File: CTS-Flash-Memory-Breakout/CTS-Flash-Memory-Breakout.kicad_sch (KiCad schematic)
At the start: 8 parts, among them J1 Conn_02x07_Counter_Clockwise, U1 S70FL01GSAGMFI011

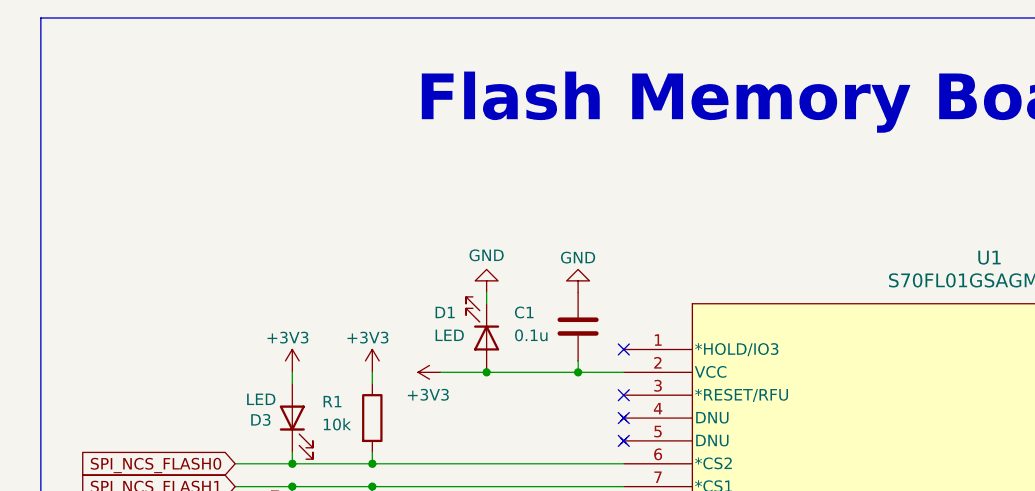
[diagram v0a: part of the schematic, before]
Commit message: Update errata on schematic, add rendering and part number to README
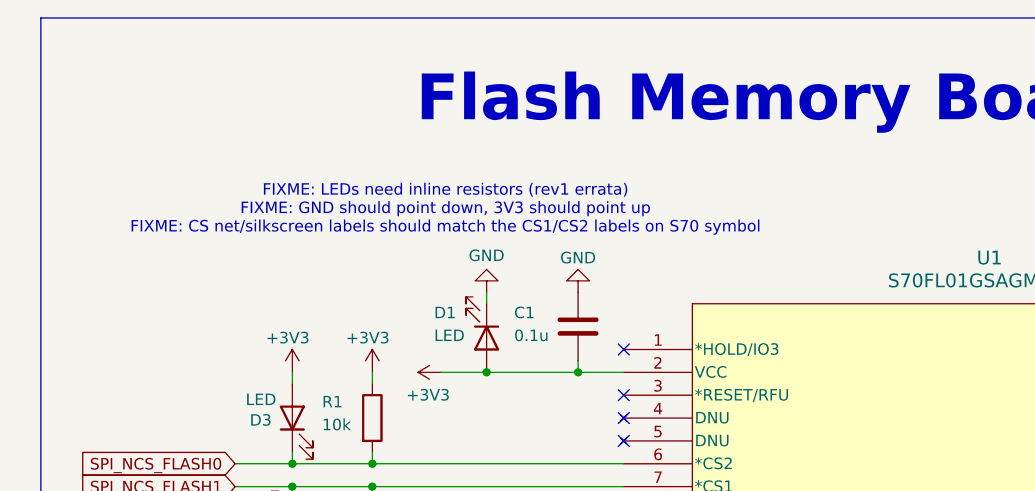
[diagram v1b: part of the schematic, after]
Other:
- note added: "FIXME: LEDs need inline resistors (rev1 errata) FIXME: GND should point down, 3V3 should point up FIXME: CS net/silkscreen labels should match the CS1/CS2 labels on S70 symbol"
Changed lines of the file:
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@@
 	(generator "eeschema")
 	(generator_version "8.0")
-	(paper "A4")
+	(paper "USLetter")
+	(title_block
+		(rev "rev1")
+	)
 	(junction
 		(at 116.84 72.39)
@@
 			)
 		)
+	)
+	(text "FIXME: LEDs need inline resistors (rev1 errata)\nFIXME: GND should point down, 3V3 should point up\nFIXME: CS net/silkscreen labels should match the CS1/CS2 labels on S70 symbol"
+		(exclude_from_sim no)
+		(at 112.268 54.356 0)
+		(effects
+			(font
+				(size 1.27 1.27)
+			)
+		)

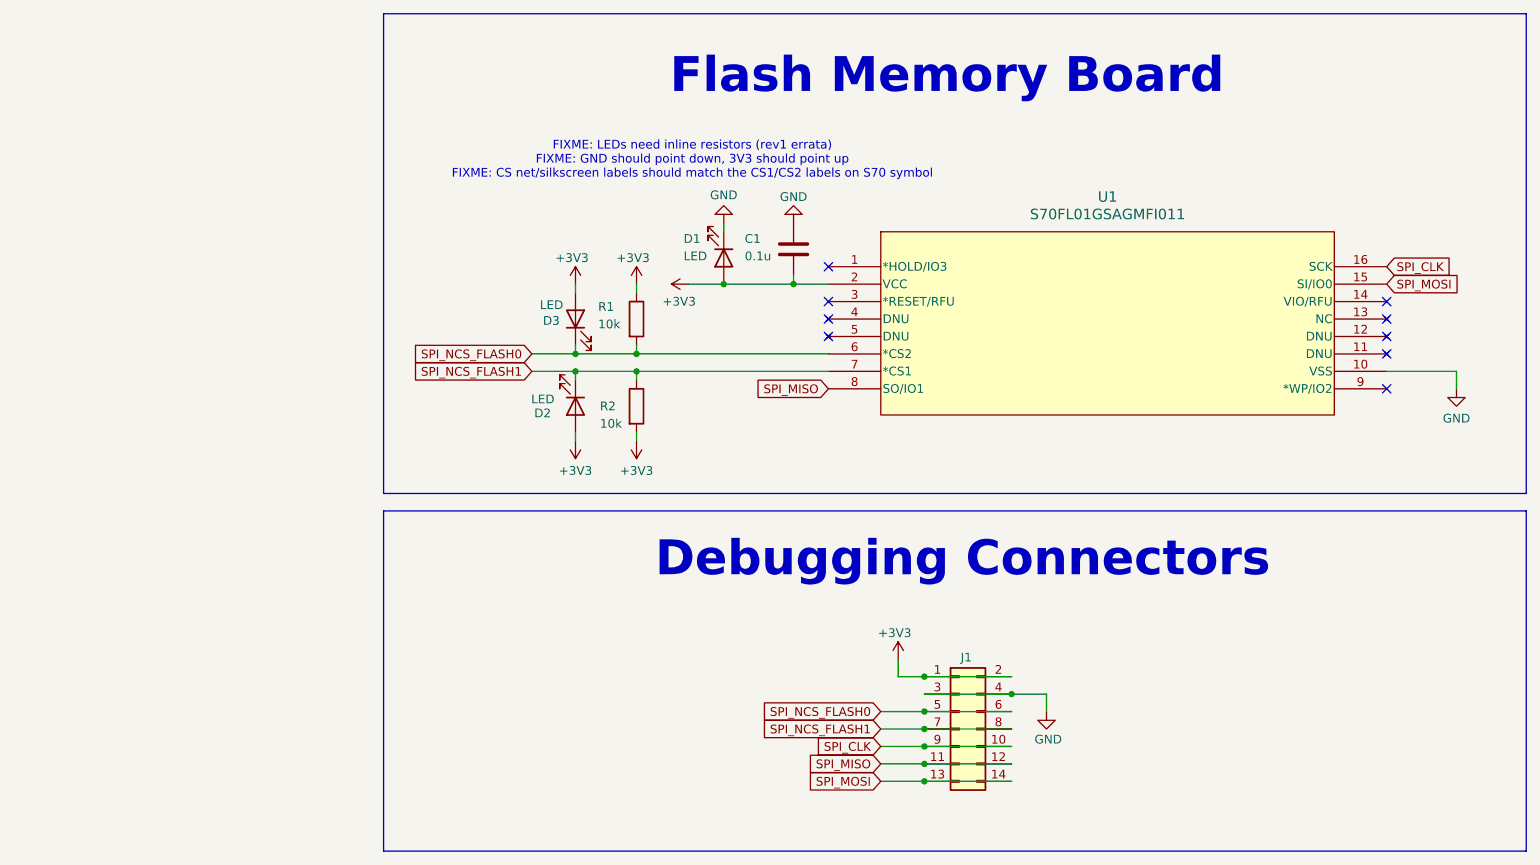
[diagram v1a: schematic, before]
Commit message: Create Rev 2 board
- Breakout every pin on the chip to new headers
- Fix missing inline resistors for LEDs
- Add extra bulk capacitance
- Reroute with wide traces
- More silkscreens
- Silkscreens for writing notes/labels in Sharpie
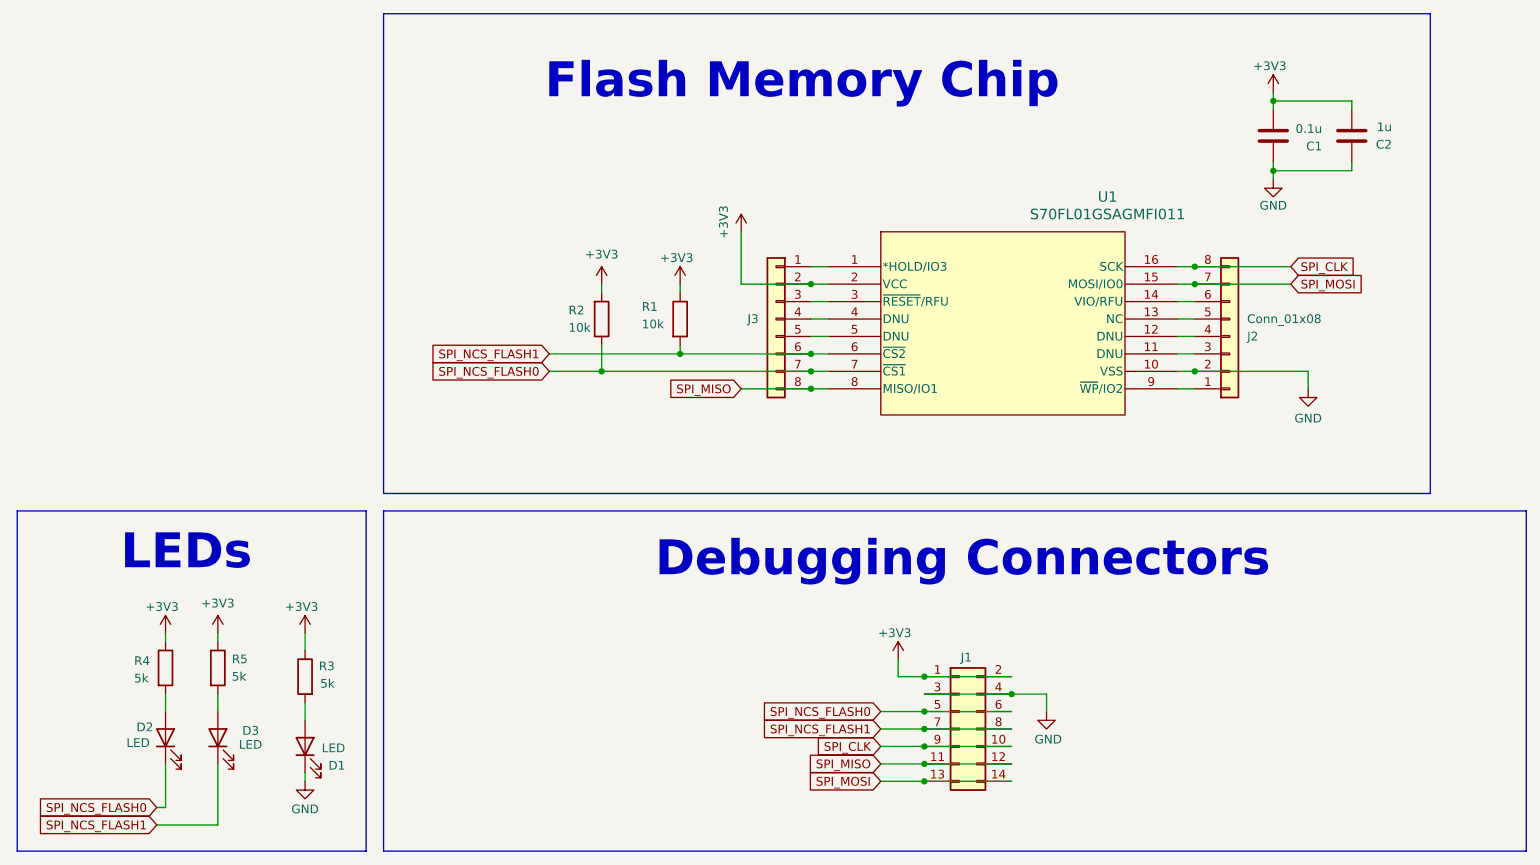
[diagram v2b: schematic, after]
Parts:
- added C2: 1u, Capacitor_SMD:C_1206_3216Metric_Pad1.33x1.80mm_HandSolder, symbol Device:C
- added J2, J3: Conn_01x08, Connector_PinHeader_2.54mm:PinHeader_1x08_P2.54mm_Vertical, symbol Connector_Generic:Conn_01x08
- added R3, R4, R5: 5k, Resistor_SMD:R_1206_3216Metric_Pad1.30x1.75mm_HandSolder, symbol Device:R
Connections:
- net +3V3: now also C2.2, J3.2 (Pin_2), R3.1, R4.1, R5.1; no longer D1.2 (A), D2.2 (A), D3.2 (A)
- net GND: now also C2.1, J2.2 (Pin_2)
- net SPI_CLK: now also J2.8 (Pin_8)
- net SPI_MISO: now also J3.8 (Pin_8)
- net SPI_MOSI: now also J2.7 (Pin_7)
- net SPI_NCS_FLASH0: now also D2.1 (K), R2.1, U1.7 (~{CS1}), J3.7 (Pin_7); no longer D3.1 (K), R1.2, U1.6 (*CS2)
- net SPI_NCS_FLASH1: now also D3.1 (K), R1.2, U1.6 (~{CS2}), J3.6 (Pin_6); no longer D2.1 (K), R2.1, U1.7 (*CS1)
- net at U1.1 (*HOLD/IO3): now also J3.1 (Pin_1)
- net at U1.11 (DNU): now also J2.3 (Pin_3)
- net at U1.12 (DNU): now also J2.4 (Pin_4)
- net at U1.13 (NC): now also J2.5 (Pin_5)
- net at U1.14 (VIO/RFU): now also J2.6 (Pin_6)
- net at U1.3 (~{RESET}/RFU): now also J3.3 (Pin_3)
- net at U1.4 (DNU): now also J3.4 (Pin_4)
- net at U1.5 (DNU): now also J3.5 (Pin_5)
- net at U1.9 (~{WP}/IO2): now also J2.1 (Pin_1)
- new net: D1.2 (A), R3.2
- new net: D3.2 (A), R5.2
- new net: D2.2 (A), R4.2
- no-connect marks 9 -> 0
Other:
- note added: "Flash Memory Chip"
- note added: "LEDs"
- note removed: "FIXME: LEDs need inline resistors (rev1 errata) FIXME: GND should point down, 3V3 should point up FIXME: CS net/silkscreen labels should match the CS1/CS2 labels on S70 symbol"
- note removed: "Flash Memory Board"
- title: (none) -> S70FL01GSAGMFI011 Breakout Board
- moved on the sheet: C1, D1, R1, R2

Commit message: Create Rev 2
- Add mounting holes
- Improve routing
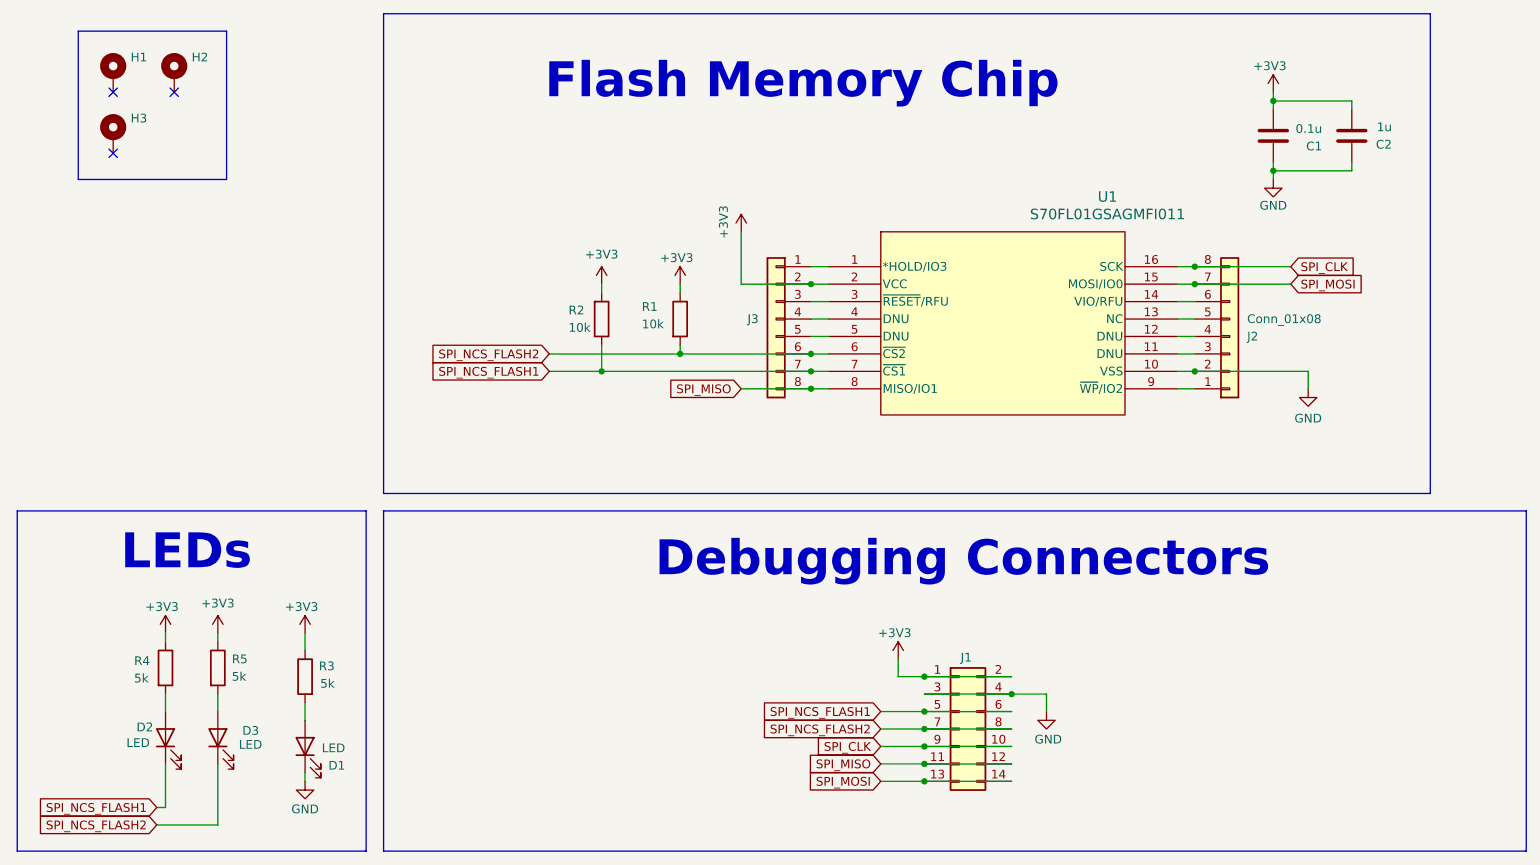
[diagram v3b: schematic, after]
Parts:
- added H1, H2, H3: MountingHole_Pad, MountingHole:MountingHole_2.2mm_M2_DIN965_Pad, symbol Mechanical:MountingHole_Pad
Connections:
- net SPI_NCS_FLASH0 is gone; now on net SPI_NCS_FLASH1: D2.1 (K), J1.5 (Pin_5), J1.6 (Pin_6), J3.7 (Pin_7), R2.1, U1.7 (~{CS1})
- net SPI_NCS_FLASH1: no longer D3.1 (K), J1.7 (Pin_7), J1.8 (Pin_8), J3.6 (Pin_6), R1.2, U1.6 (~{CS2})
- new net SPI_NCS_FLASH2: D3.1 (K), J1.7 (Pin_7), J1.8 (Pin_8), J3.6 (Pin_6), R1.2, U1.6 (~{CS2})
- no-connect marks 0 -> 3
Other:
- title: S70FL01GSAGMFI011 Breakout Board -> Flash Module Breakout Board
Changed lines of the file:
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@@
 	(paper "USLetter")
 	(title_block
-		(title "S70FL01GSAGMFI011 Breakout Board")
-		(date "2024-06-08")
+		(title "Flash Module Breakout Board")
+		(date "2024-06-21")
 		(rev "Rev 2")
 	)
@@
 		(color 0 0 0 0)
 	)
+	(no_connect
+		(at 36.83 44.45)
+	)
+	(no_connect
+		(at 27.94 53.34)
+	)
+	(no_connect
+		(at 27.94 44.45)
+	)
 	(wire
 		(pts
@@
 		(start 67.31 33.02)
 		(end 219.71 102.87)
+		(stroke
+			(width 0)
+			(type default)
+		)
+		(fill
+			(type none)
+		)
+	)
+	(rectangle
+		(start 22.86 35.56)
+		(end 44.45 57.15)
 		(stroke
 			(width 0)
@@
 		)
 	)
-	(global_label "SPI_NCS_FLASH1"
+	(global_label "SPI_NCS_FLASH2"
 		(shape input)
 		(at 34.29 151.13 180)
@@
 		)
 	)
-	(global_label "SPI_NCS_FLASH0"
+	(global_label "SPI_NCS_FLASH1"
 		(shape input)
 		(at 139.7 134.62 180)
@@
 		)
 	)
-	(global_label "SPI_NCS_FLASH0"
+	(global_label "SPI_NCS_FLASH1"
 		(shape input)
 		(at 34.29 148.59 180)
@@
 		)
 	)
-	(global_label "SPI_NCS_FLASH0"
+	(global_label "SPI_NCS_FLASH1"
 		(shape input)
 		(at 91.44 85.09 180)
@@
 		)
 	)
-	(global_label "SPI_NCS_FLASH1"
+	(global_label "SPI_NCS_FLASH2"
 		(shape input)
 		(at 91.44 82.55 180)
@@
 		)
 	)
-	(global_label "SPI_NCS_FLASH1"
+	(global_label "SPI_NCS_FLASH2"
 		(shape input)
 		(at 139.7 137.16 180)
@@
 	)
 	(symbol
+		(lib_id "Mechanical:MountingHole_Pad")
+		(at 36.83 41.91 0)
+		(unit 1)
+		(exclude_from_sim yes)
+		(in_bom no)
+		(on_board yes)
+		(dnp no)
+		(fields_autoplaced yes)
+		(property "Reference" "H2"
+			(at 39.37 39.3699 0)
+			(effects
+				(font
+					(size 1.27 1.27)
+				)
+				(justify left)
+			)
+		)
+		(property "Value" "MountingHole_Pad"
+			(at 39.37 41.9099 0)
+			(effects
+				(font
+					(size 1.27 1.27)
+				)
+				(justify left)
+				(hide yes)
+			)
+		)
+		(property "Footprint" "MountingHole:MountingHole_2.2mm_M2_DIN965_Pad"
+			(at 36.83 41.91 0)
+			(effects
+				(font
+					(size 1.27 1.27)
+				)
+				(hide yes)
+			)
+		)
+		(property "Datasheet" "~"
+			(at 36.83 41.91 0)
+			(effects
+				(font
+					(size 1.27 1.27)
+				)
+				(hide yes)
+			)
+		)
+		(property "Description" "Mounting Hole with connection"
+			(at 36.83 41.91 0)
+			(effects
+				(font
+					(size 1.27 1.27)
+				)
+				(hide yes)
+			)
+		)
+		(pin "1"
+		)
+		(instances
+			(project "CTS-Flash-Memory-Breakout"
+				(path "/9d2a0b6c-cc79-41b3-8be4-5e021c4ca4aa"
+					(reference "H2")
+					(unit 1)
+				)
+			)
+		)
+	)
+	(symbol
 		(lib_id "Device:R")
 		(at 110.49 77.47 0)
@@
 	)
 	(symbol
+		(lib_id "Mechanical:MountingHole_Pad")
+		(at 27.94 50.8 0)
+		(unit 1)
+		(exclude_from_sim yes)
+		(in_bom no)
+		(on_board yes)
+		(dnp no)
+		(fields_autoplaced yes)
+		(property "Reference" "H3"
+			(at 30.48 48.2599 0)
+			(effects
+				(font
+					(size 1.27 1.27)
+				)
+				(justify left)
+			)
+		)
+		(property "Value" "MountingHole_Pad"
+			(at 30.48 50.7999 0)
+			(effects
+				(font
+					(size 1.27 1.27)
+				)
+				(justify left)
+				(hide yes)
+			)
+		)
+		(property "Footprint" "MountingHole:MountingHole_2.2mm_M2_DIN965_Pad"
+			(at 27.94 50.8 0)
+			(effects
+				(font
+					(size 1.27 1.27)
+				)
+				(hide yes)
+			)
+		)
+		(property "Datasheet" "~"
+			(at 27.94 50.8 0)
+			(effects
+				(font
+					(size 1.27 1.27)
+				)
+				(hide yes)
+			)
+		)
+		(property "Description" "Mounting Hole with connection"
+			(at 27.94 50.8 0)
+			(effects
+				(font
+					(size 1.27 1.27)
+				)
+				(hide yes)
+			)
+		)
+		(pin "1"
+		)
+		(instances
+			(project "CTS-Flash-Memory-Breakout"
+				(path "/9d2a0b6c-cc79-41b3-8be4-5e021c4ca4aa"
+					(reference "H3")
+					(unit 1)
+				)
+			)
+		)
+	)
+	(symbol
 		(lib_id "Connector_Generic:Conn_01x08")
 		(at 190.5 80.01 0)
@@
 					(unit 1)
 				)
+			)
+		)
+	)
+	(symbol
+		(lib_id "Mechanical:MountingHole_Pad")
+		(at 27.94 41.91 0)
+		(unit 1)
+		(exclude_from_sim yes)
+		(in_bom no)
+		(on_board yes)
+		(dnp no)
+		(fields_autoplaced yes)
+		(property "Reference" "H1"
+			(at 30.48 39.3699 0)
+			(effects
+				(font
+					(size 1.27 1.27)
+				)
+				(justify left)
+			)
+		)
+		(property "Value" "MountingHole_Pad"
+			(at 30.48 41.9099 0)
+			(effects
+				(font
+					(size 1.27 1.27)
+				)
+				(justify left)
+				(hide yes)
+			)
+		)
+		(property "Footprint" "MountingHole:MountingHole_2.2mm_M2_DIN965_Pad"
+			(at 27.94 41.91 0)
+			(effects
+				(font
+					(size 1.27 1.27)
+				)
+				(hide yes)
+			)
+		)
+		(property "Datasheet" "~"
+			(at 27.94 41.91 0)
+			(effects
+				(font
+					(size 1.27 1.27)
+				)
+				(hide yes)
+			)
+		)
+		(property "Description" "Mounting Hole with connection"
+			(at 27.94 41.91 0)
+			(effects
+				(font
+					(size 1.27 1.27)
+				)
+				(hide yes)
+			)
+		)
+		(pin "1"
+		)
+		(instances
+			(project ""
+				(path "/9d2a0b6c-cc79-41b3-8be4-5e021c4ca4aa"
+					(reference "H1")
+					(unit 1)
+				)

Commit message: Re-plot Rev 3 schematic
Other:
- note added: "Any resistor value from 3k3 to 10k can be used."
- note added: "Any resistor value from 3k3 to 8k can be used."
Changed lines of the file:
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@@
+		)
+	)
+	(text "Any resistor value from\n3k3 to 10k can be used."
+		(exclude_from_sim no)
+		(at 101.346 63.754 0)
+		(effects
+			(font
+				(size 1.27 1.27)
+			)
+		)
+	)
+	(text "Any resistor value from\n3k3 to 8k can be used."
+		(exclude_from_sim no)
+		(at 24.892 129.286 90)
+		(effects
+			(font
+				(size 1.27 1.27)
+			)
 		)
 	)
